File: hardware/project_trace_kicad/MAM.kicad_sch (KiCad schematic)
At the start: 2 parts, among them U501 NUCLEO-H753ZI

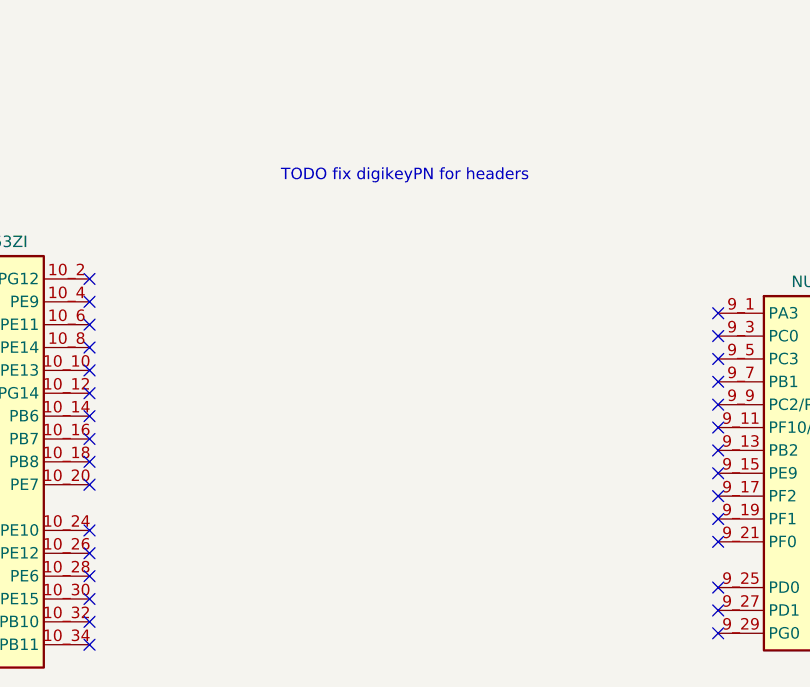
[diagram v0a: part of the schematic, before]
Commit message: Symbols for Pin-ordering added to MAM
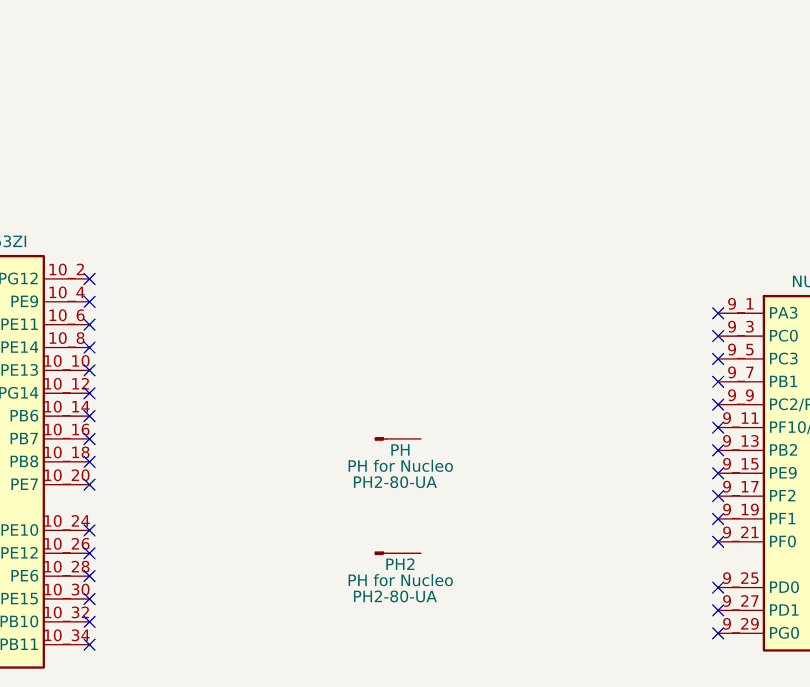
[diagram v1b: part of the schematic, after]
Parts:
- added PH, PH2: PH for Nucleo, symbol Connector:Conn_01x01_Pin
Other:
- note removed: "TODO fix digikeyPN for headers"
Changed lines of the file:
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@@
 		(company "Alexander N. Olsen")
-	)
-	(text "TODO fix digikeyPN for headers\n"
-		(exclude_from_sim no)
-		(at 129.032 95.25 0)
-		(effects
-			(font
-				(size 1.27 1.27)
-			)
-		)
 	)
 	(junction
@@
 	)
 	(symbol
+		(lib_name "Conn_01x01_Pin_1")
+		(lib_id "Connector:Conn_01x01_Pin")
+		(at 125.73 137.16 0)
+		(unit 1)
+		(body_style 1)
+		(exclude_from_sim no)
+		(in_bom yes)
+		(on_board no)
+		(in_pos_files yes)
+		(dnp no)
+		(property "Reference" "PH2"
+			(at 128.524 138.43 0)
+			(show_name no)
+			(do_not_autoplace no)
+			(effects
+				(font
+					(size 1.27 1.27)
+				)
+			)
+		)
+		(property "Value" "PH for Nucleo"
+			(at 128.524 140.208 0)
+			(show_name no)
+			(do_not_autoplace no)
+			(effects
+				(font
+					(size 1.27 1.27)
+				)
+			)
+		)
+		(property "Footprint" ""
+			(at 125.73 137.16 0)
+			(hide yes)
+			(show_name no)
+			(do_not_autoplace no)
+			(effects
+				(font
+					(size 1.27 1.27)
+				)
+			)
+		)
+		(property "Datasheet" ""
+			(at 125.73 137.16 0)
+			(hide yes)
+			(show_name no)
+			(do_not_autoplace no)
+			(effects
+				(font
+					(size 1.27 1.27)
+				)
+			)
+		)
+		(property "Description" "PH2-80-UA"
+			(at 127.889 142.0044 0)
+			(show_name no)
+			(do_not_autoplace no)
+			(effects
+				(font
+					(size 1.27 1.27)
+				)
+			)
+		)
+		(property "DIgikeyPN" "2057-PH2-80-UA-ND"
+			(at 125.73 137.16 0)
+			(hide yes)
+			(show_name no)
+			(do_not_autoplace no)
+			(effects
+				(font
+					(size 1.27 1.27)
+				)
+			)
+		)
+		(pin "1"
+		)
+		(instances
+			(project "project_trace_kicad"
+				(path "/af51f4e5-b952-4b0e-baf2-78a72fb86fcd/aebaf62e-54ce-46f5-a91f-d86d07c0b2fa"
+					(reference "PH2")
+					(unit 1)
+				)
+			)
+		)
+	)
+	(symbol
 		(lib_name "NUCLEO-H753ZI_Module_2")
 		(lib_id "ProjectTraceSymbols:NUCLEO-H753ZI_Module")
@@
 				)
 			)
+		)
+	)
+	(symbol
+		(lib_id "Connector:Conn_01x01_Pin")
+		(at 125.73 124.46 0)
+		(unit 1)
+		(body_style 1)
+		(exclude_from_sim no)
+		(in_bom yes)
+		(on_board no)
+		(in_pos_files yes)
+		(dnp no)
+		(property "Reference" "PH"
+			(at 128.524 125.73 0)
+			(show_name no)
+			(do_not_autoplace no)
+			(effects
+				(font
+					(size 1.27 1.27)
+				)
+			)
+		)
+		(property "Value" "PH for Nucleo"
+			(at 128.524 127.508 0)
+			(show_name no)
+			(do_not_autoplace no)
+			(effects
+				(font
+					(size 1.27 1.27)
+				)
+			)
+		)
+		(property "Footprint" ""
+			(at 125.73 124.46 0)
+			(hide yes)
+			(show_name no)
+			(do_not_autoplace no)
+			(effects
+				(font
+					(size 1.27 1.27)
+				)
+			)
+		)
+		(property "Datasheet" ""
+			(at 125.73 124.46 0)
+			(hide yes)
+			(show_name no)
+			(do_not_autoplace no)
+			(effects
+				(font
+					(size 1.27 1.27)
+				)
+			)
+		)
+		(property "Description" "PH2-80-UA"
+			(at 127.889 129.3044 0)
+			(show_name no)
+			(do_not_autoplace no)
+			(effects
+				(font
+					(size 1.27 1.27)
+				)
+			)
+		)
+		(property "DIgikeyPN" "2057-PH2-80-UA-ND"
+			(at 125.73 124.46 0)
+			(hide yes)
+			(show_name no)
+			(do_not_autoplace no)
+			(effects
+				(font
+					(size 1.27 1.27)
+				)
+			)
+		)
+		(pin "1"
+		)
+		(instances
+			(project "project_trace_kicad"
+				(path "/af51f4e5-b952-4b0e-baf2-78a72fb86fcd/aebaf62e-54ce-46f5-a91f-d86d07c0b2fa"
+					(reference "PH")
+					(unit 1)
+				)
+			)

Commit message: Work on PCB
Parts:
- renumbered PH to PH501, PH2 to PH502
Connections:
- no-connect marks 67 -> 69
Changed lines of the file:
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@@
+	)
+	(no_connect
+		(at 130.81 124.46)
 	)
 	(no_connect
@@
 	(no_connect
 		(at 194.31 128.27)
+	)
+	(no_connect
+		(at 130.81 137.16)
 	)
 	(no_connect
@@
 		(in_pos_files yes)
 		(dnp no)
-		(property "Reference" "PH2"
+		(property "Reference" "PH502"
 			(at 128.524 138.43 0)
 			(show_name no)
@@
 			(project "project_trace_kicad"
 				(path "/af51f4e5-b952-4b0e-baf2-78a72fb86fcd/aebaf62e-54ce-46f5-a91f-d86d07c0b2fa"
-					(reference "PH2")
+					(reference "PH502")
 					(unit 1)
 				)
@@
 		(in_pos_files yes)
 		(dnp no)
-		(property "Reference" "PH"
+		(property "Reference" "PH501"
 			(at 128.524 125.73 0)
 			(show_name no)
@@
 			(project "project_trace_kicad"
 				(path "/af51f4e5-b952-4b0e-baf2-78a72fb86fcd/aebaf62e-54ce-46f5-a91f-d86d07c0b2fa"
-					(reference "PH")
+					(reference "PH501")
 					(unit 1)
 				)

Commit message: Partnumbers and BOM updated
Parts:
- PH501, PH502: DIgikeyPN 2057-PH2-80-UA-ND -> (none); DigikeyPN (none) -> 2057-PH2-80-UA-ND
- U501: DigikeyPN 2057-PH2-80-UA-ND AND 2057-PH2-20-UA-ND -> (none)
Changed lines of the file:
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@@
-			)
-		)
-		(property "DigikeyPN" "2057-PH2-80-UA-ND AND 2057-PH2-20-UA-ND"
-			(at 77.47 49.53 0)
-			(hide yes)
-			(show_name no)
-			(do_not_autoplace no)
-			(effects
-				(font
-					(size 1.27 1.27)
-				)
 			)
 		)
@@
 			)
 		)
-		(property "DIgikeyPN" "2057-PH2-80-UA-ND"
+		(property "DigikeyPN" "2057-PH2-80-UA-ND"
 			(at 125.73 137.16 0)
 			(hide yes)
@@
 			)
 		)
-		(property "DigikeyPN" "2057-PH2-80-UA-ND AND 2057-PH2-20-UA-ND"
-			(at 179.07 128.27 0)
-			(hide yes)
-			(show_name no)
-			(do_not_autoplace no)
-			(effects
-				(font
-					(size 1.27 1.27)
-				)
-			)
-		)
 		(pin "9_12"
 		)
@@
 		(property "Description" "Nucleo 144 Development Board with STM32F429ZIT6 MCU, 256kB RAM, 1Mb FLASH"
 			(at 147.32 -49.53 0)
-			(hide yes)
-			(show_name no)
-			(do_not_autoplace no)
-			(effects
-				(font
-					(size 1.27 1.27)
-				)
-			)
-		)
-		(property "DigikeyPN" "2057-PH2-80-UA-ND AND 2057-PH2-20-UA-ND"
-			(at 147.32 52.07 0)
 			(hide yes)
 			(show_name no)
@@
 			)
 		)
-		(property "DigikeyPN" "2057-PH2-80-UA-ND AND 2057-PH2-20-UA-ND"
-			(at 80.01 127 0)
-			(hide yes)
-			(show_name no)
-			(do_not_autoplace no)
-			(effects
-				(font
-					(size 1.27 1.27)
-				)
-			)
-		)
 		(pin "9_12"
 		)
@@
 			)
 		)
-		(property "DigikeyPN" "2057-PH2-80-UA-ND AND 2057-PH2-20-UA-ND"
-			(at 213.36 55.88 0)
-			(hide yes)
-			(show_name no)
-			(do_not_autoplace no)
-			(effects
-				(font
-					(size 1.27 1.27)
-				)
-			)
-		)
 		(pin "9_12"
 		)
@@
 			)
 		)
-		(property "DIgikeyPN" "2057-PH2-80-UA-ND"
+		(property "DigikeyPN" "2057-PH2-80-UA-ND"
 			(at 125.73 124.46 0)
 			(hide yes)

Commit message: Improvements to PCB
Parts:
- R501: value 100 -> 24R9; footprint ProjectTraceFootprints:RN73R2ATTD1000B25 -> Resistor_SMD:R_0603_1608Metric_Pad0.98x0.95mm_HandSolder; DigikeyPN 2019-RN73R2ATTD1000B25CT-ND -> YAG4511CT-ND
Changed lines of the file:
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@@
+	)
+	(symbol
+		(lib_id "Device:R")
+		(at 242.57 49.53 90)
+		(unit 1)
+		(body_style 1)
+		(exclude_from_sim no)
+		(in_bom yes)
+		(on_board yes)
+		(in_pos_files yes)
+		(dnp no)
+		(fields_autoplaced yes)
+		(property "Reference" "R501"
+			(at 242.57 44.7546 90)
+			(show_name no)
+			(do_not_autoplace no)
+			(effects
+				(font
+					(size 1.27 1.27)
+				)
+			)
+		)
+		(property "Value" "24R9"
+			(at 242.57 46.9222 90)
+			(show_name no)
+			(do_not_autoplace no)
+			(effects
+				(font
+					(size 1.27 1.27)
+				)
+			)
+		)
+		(property "Footprint" "Resistor_SMD:R_0603_1608Metric_Pad0.98x0.95mm_HandSolder"
+			(at 242.57 51.308 90)
+			(hide yes)
+			(show_name no)
+			(do_not_autoplace no)
+			(effects
+				(font
+					(size 1.27 1.27)
+				)
+			)
+		)
+		(property "Datasheet" ""
+			(at 242.57 49.53 0)
+			(hide yes)
+			(show_name no)
+			(do_not_autoplace no)
+			(effects
+				(font
+					(size 1.27 1.27)
+				)
+			)
+		)
+		(property "Description" "Resistor"
+			(at 242.57 49.53 0)
+			(hide yes)
+			(show_name no)
+			(do_not_autoplace no)
+			(effects
+				(font
+					(size 1.27 1.27)
+				)
+			)
+		)
+		(property "DigikeyPN" "YAG4511CT-ND"
+			(at 242.57 49.53 90)
+			(hide yes)
+			(show_name no)
+			(do_not_autoplace no)
+			(effects
+				(font
+					(size 1.27 1.27)
+				)
+			)
+		)
+		(pin "1"
+		)
+		(pin "2"
+		)
+		(instances
+			(project "project_trace_kicad"
+				(path "/af51f4e5-b952-4b0e-baf2-78a72fb86fcd/aebaf62e-54ce-46f5-a91f-d86d07c0b2fa"
+					(reference "R501")
+					(unit 1)
+				)
+			)
+		)
 	)
 	(symbol
@@
 					(unit 1)
 				)
-			)
-		)
-	)
-	(symbol
-		(lib_id "Device:R")
-		(at 242.57 49.53 90)
-		(unit 1)
-		(body_style 1)
-		(exclude_from_sim no)
-		(in_bom yes)
-		(on_board yes)
-		(in_pos_files yes)
-		(dnp no)
-		(fields_autoplaced yes)
-		(property "Reference" "R501"
-			(at 242.57 44.3695 90)
-			(show_name no)
-			(do_not_autoplace no)
-			(effects
-				(font
-					(size 1.27 1.27)
-				)
-			)
-		)
-		(property "Value" "100"
-			(at 242.57 46.7938 90)
-			(show_name no)
-			(do_not_autoplace no)
-			(effects
-				(font
-					(size 1.27 1.27)
-				)
-			)
-		)
-		(property "Footprint" "ProjectTraceFootprints:RN73R2ATTD1000B25"
-			(at 242.57 51.308 90)
-			(hide yes)
-			(show_name no)
-			(do_not_autoplace no)
-			(effects
-				(font
-					(size 1.27 1.27)
-				)
-			)
-		)
-		(property "Datasheet" ""
-			(at 242.57 49.53 0)
-			(hide yes)
-			(show_name no)
-			(do_not_autoplace no)
-			(effects
-				(font
-					(size 1.27 1.27)
-				)
-			)
-		)
-		(property "Description" "Resistor"
-			(at 242.57 49.53 0)
-			(hide yes)
-			(show_name no)
-			(do_not_autoplace no)
-			(effects
-				(font
-					(size 1.27 1.27)
-				)
-			)
-		)
-		(property "DigikeyPN" "2019-RN73R2ATTD1000B25CT-ND"
-			(at 242.57 49.53 90)
-			(hide yes)
-			(show_name no)
-			(do_not_autoplace no)
-			(effects
-				(font
-					(size 1.27 1.27)
-				)
-			)
-		)
-		(pin "1"
-		)
-		(pin "2"
-		)
-		(instances
-			(project "project_trace_kicad"
-				(path "/af51f4e5-b952-4b0e-baf2-78a72fb86fcd/aebaf62e-54ce-46f5-a91f-d86d07c0b2fa"
-					(reference "R501")
-					(unit 1)
-				)

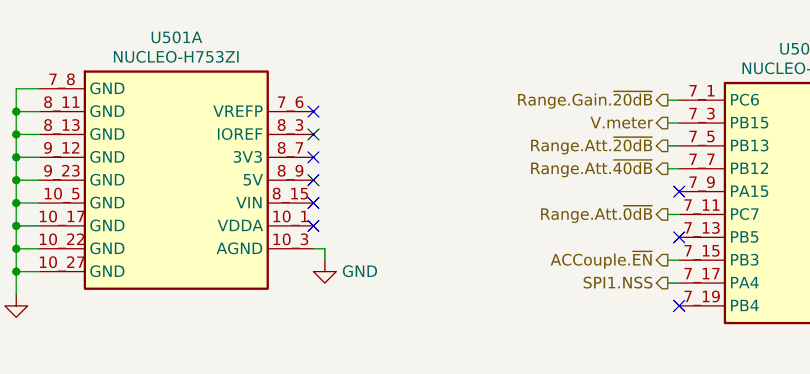
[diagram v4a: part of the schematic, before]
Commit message: Add Missing Power Connection to Nucleo
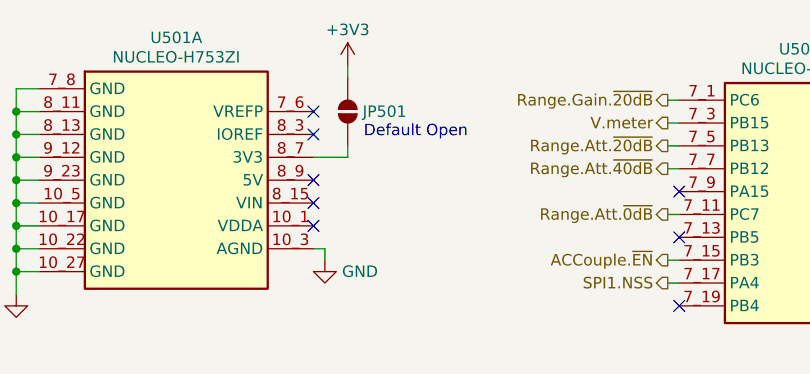
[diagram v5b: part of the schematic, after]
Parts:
- added JP501: SolderJumper_2_Open, Jumper:SolderJumper-2_P1.3mm_Open_RoundedPad1.0x1.5mm, symbol Jumper:SolderJumper_2_Open
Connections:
- net at U501.8_7 (3V3): now also JP501.2 (B)
- new net +3V3: JP501.1 (A)
- no-connect marks 69 -> 68
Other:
- note added: "Default Open"
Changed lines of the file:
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@@
 		(company "Alexander N. Olsen")
+	)
+	(text "Default Open"
+		(exclude_from_sim no)
+		(at 98.298 44.196 0)
+		(effects
+			(font
+				(size 1.27 1.27)
+			)
+			(justify left)
+		)
 	)
 	(junction
@@
 	)
 	(no_connect
-		(at 92.71 46.99)
-	)
-	(no_connect
 		(at 161.29 43.18)
 	)
@@
 	(wire
 		(pts
+			(xy 96.52 36.83) (xy 96.52 38.1)
+		)
+		(stroke
+			(width 0)
+			(type default)
+		)
+	)
+	(wire
+		(pts
 			(xy 59.69 54.61) (xy 59.69 57.15)
 		)
@@
 	(wire
 		(pts
+			(xy 96.52 45.72) (xy 96.52 46.99)
+		)
+		(stroke
+			(width 0)
+			(type default)
+		)
+	)
+	(wire
+		(pts
 			(xy 227.33 49.53) (xy 238.76 49.53)
 		)
@@
 		(pts
 			(xy 59.69 39.37) (xy 62.23 39.37)
+		)
+		(stroke
+			(width 0)
+			(type default)
+		)
+	)
+	(wire
+		(pts
+			(xy 96.52 46.99) (xy 92.71 46.99)
 		)
 		(stroke
@@
 				(path "/af51f4e5-b952-4b0e-baf2-78a72fb86fcd/aebaf62e-54ce-46f5-a91f-d86d07c0b2fa"
 					(reference "R501")
+					(unit 1)
+				)
+			)
+		)
+	)
+	(symbol
+		(lib_id "Jumper:SolderJumper_2_Open")
+		(at 96.52 41.91 270)
+		(unit 1)
+		(body_style 1)
+		(exclude_from_sim no)
+		(in_bom no)
+		(on_board yes)
+		(in_pos_files yes)
+		(dnp no)
+		(fields_autoplaced yes)
+		(property "Reference" "JP501"
+			(at 98.171 41.91 90)
+			(show_name no)
+			(do_not_autoplace no)
+			(effects
+				(font
+					(size 1.27 1.27)
+				)
+				(justify left)
+			)
+		)
+		(property "Value" "SolderJumper_2_Open"
+			(at 94.869 40.8262 90)
+			(hide yes)
+			(show_name no)
+			(do_not_autoplace no)
+			(effects
+				(font
+					(size 1.27 1.27)
+				)
+				(justify right)
+			)
+		)
+		(property "Footprint" "Jumper:SolderJumper-2_P1.3mm_Open_RoundedPad1.0x1.5mm"
+			(at 96.52 41.91 0)
+			(hide yes)
+			(show_name no)
+			(do_not_autoplace no)
+			(effects
+				(font
+					(size 1.27 1.27)
+				)
+			)
+		)
+		(property "Datasheet" ""
+			(at 96.52 41.91 0)
+			(hide yes)
+			(show_name no)
+			(do_not_autoplace no)
+			(effects
+				(font
+					(size 1.27 1.27)
+				)
+			)
+		)
+		(property "Description" "Solder Jumper, 2-pole, open"
+			(at 96.52 41.91 0)
+			(hide yes)
+			(show_name no)
+			(do_not_autoplace no)
+			(effects
+				(font
+					(size 1.27 1.27)
+				)
+			)
+		)
+		(property "DigikeyPN" "N/A"
+			(at 96.52 41.91 90)
+			(hide yes)
+			(show_name no)
+			(do_not_autoplace no)
+			(effects
+				(font
+					(size 1.27 1.27)
+				)
+			)
+		)
+		(pin "1"
+		)
+		(pin "2"
+		)
+		(instances
+			(project "project_trace_kicad"
+				(path "/af51f4e5-b952-4b0e-baf2-78a72fb86fcd/aebaf62e-54ce-46f5-a91f-d86d07c0b2fa"
+					(reference "JP501")
 					(unit 1)
 				)
@@
 					(unit 1)
 				)
+			)
+		)
+	)
+	(symbol
+		(lib_id "power:+3V3")
+		(at 96.52 36.83 0)
+		(unit 1)
+		(body_style 1)
+		(exclude_from_sim no)
+		(in_bom yes)
+		(on_board yes)
+		(in_pos_files yes)
+		(dnp no)
+		(fields_autoplaced yes)
+		(property "Reference" "#PWR0503"
+			(at 96.52 40.64 0)
+			(hide yes)
+			(show_name no)
+			(do_not_autoplace no)
+			(effects
+				(font
+					(size 1.27 1.27)
+				)
+			)
+		)
+		(property "Value" "+3V3"
+			(at 96.52 32.8252 0)
+			(show_name no)
+			(do_not_autoplace no)
+			(effects
+				(font
+					(size 1.27 1.27)
+				)
+			)
+		)
+		(property "Footprint" ""
+			(at 96.52 36.83 0)
+			(hide yes)
+			(show_name no)
+			(do_not_autoplace no)
+			(effects
+				(font
+					(size 1.27 1.27)
+				)
+			)
+		)
+		(property "Datasheet" ""
+			(at 96.52 36.83 0)
+			(hide yes)
+			(show_name no)
+			(do_not_autoplace no)
+			(effects
+				(font
+					(size 1.27 1.27)
+				)
+			)
+		)
+		(property "Description" "Power symbol creates a global label with name \"+3V3\""
+			(at 96.52 36.83 0)
+			(hide yes)
+			(show_name no)
+			(do_not_autoplace no)
+			(effects
+				(font
+					(size 1.27 1.27)
+				)
+			)
+		)
+		(pin "1"
+		)
+		(instances
+			(project "project_trace_kicad"
+				(path "/af51f4e5-b952-4b0e-baf2-78a72fb86fcd/aebaf62e-54ce-46f5-a91f-d86d07c0b2fa"
+					(reference "#PWR0503")
+					(unit 1)
+				)

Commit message: Rework started
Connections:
- net SW3.A: now also U501.7_12 (PA6); no longer U501.9_24 (PF8)
- net SW3.B: now also U501.9_7 (PB1); no longer U501.9_26 (PF7)
- net SW4.A: now also U501.10_33 (PE0); no longer U501.9_28 (PF9)
- net SW4.B: now also U501.9_1 (PA3); no longer U501.9_30 (PG1)
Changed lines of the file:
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@@
-	)
-	(no_connect
-		(at 161.29 53.34)
 	)
 	(no_connect
@@
 	)
 	(no_connect
-		(at 66.04 139.7)
-	)
-	(no_connect
 		(at 93.98 114.3)
 	)
@@
 	)
 	(no_connect
+		(at 194.31 138.43)
+	)
+	(no_connect
 		(at 163.83 123.19)
 	)
@@
 	)
 	(no_connect
-		(at 163.83 110.49)
-	)
-	(no_connect
 		(at 194.31 113.03)
 	)
@@
 	)
 	(no_connect
+		(at 194.31 143.51)
+	)
+	(no_connect
 		(at 161.29 63.5)
 	)
@@
 	)
 	(no_connect
+		(at 194.31 140.97)
+	)
+	(no_connect
 		(at 66.04 134.62)
 	)
@@
 	)
 	(no_connect
-		(at 163.83 118.11)
+		(at 194.31 146.05)
 	)
 	(no_connect
@@
 	(wire
 		(pts
-			(xy 194.31 138.43) (xy 198.12 138.43)
+			(xy 161.29 53.34) (xy 163.83 53.34)
 		)
 		(stroke
@@
 	(wire
 		(pts
-			(xy 194.31 143.51) (xy 198.12 143.51)
+			(xy 66.04 139.7) (xy 64.77 139.7)
 		)
 		(stroke
@@
 	(wire
 		(pts
-			(xy 194.31 140.97) (xy 198.12 140.97)
+			(xy 163.83 118.11) (xy 162.56 118.11)
 		)
 		(stroke
@@
 	(wire
 		(pts
-			(xy 194.31 146.05) (xy 198.12 146.05)
+			(xy 163.83 110.49) (xy 162.56 110.49)
 		)
 		(stroke
@@
 	(hierarchical_label "SW4.A"
 		(shape input)
-		(at 198.12 143.51 0)
-		(effects
-			(font
-				(size 1.27 1.27)
-			)
-			(justify left)
+		(at 64.77 139.7 180)
+		(effects
+			(font
+				(size 1.27 1.27)
+			)
+			(justify right)
 		)
 	)
@@
 	(hierarchical_label "SW3.B"
 		(shape input)
-		(at 198.12 140.97 0)
-		(effects
-			(font
-				(size 1.27 1.27)
-			)
-			(justify left)
+		(at 162.56 118.11 180)
+		(effects
+			(font
+				(size 1.27 1.27)
+			)
+			(justify right)
 		)
 	)
@@
 	(hierarchical_label "SW4.B"
 		(shape input)
-		(at 198.12 146.05 0)
-		(effects
-			(font
-				(size 1.27 1.27)
-			)
-			(justify left)
+		(at 162.56 110.49 180)
+		(effects
+			(font
+				(size 1.27 1.27)
+			)
+			(justify right)
 		)
 	)
 	(hierarchical_label "SW3.A"
 		(shape input)
-		(at 198.12 138.43 0)
-		(effects
-			(font
+		(at 163.83 53.34 0)
+		(effects
+			(font

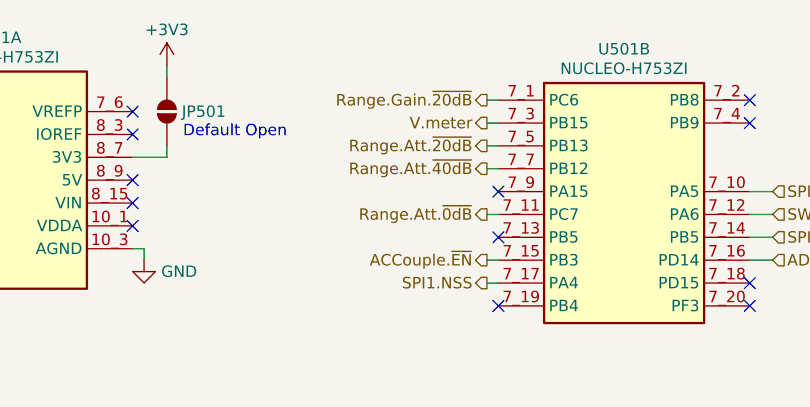
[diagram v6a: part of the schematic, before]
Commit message: Fix inconsistency with ADC datasheet, fix DRC Errors
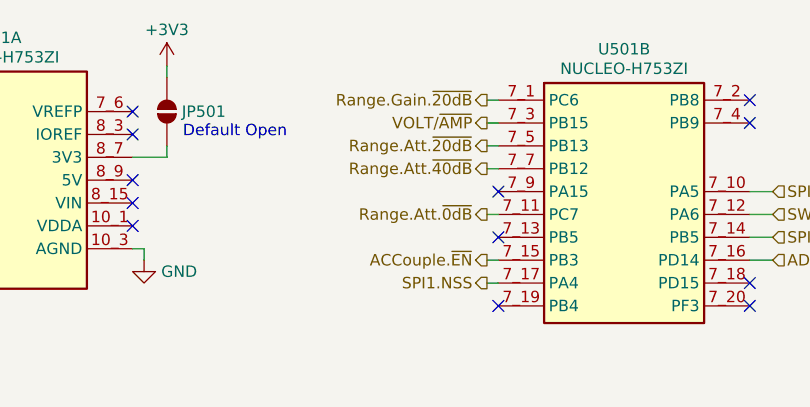
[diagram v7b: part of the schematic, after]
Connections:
- net V.meter renamed VOLT/~{AMP}
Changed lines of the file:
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@@
 		)
 	)
-	(hierarchical_label "V.meter"
+	(hierarchical_label "VOLT{slash}~{AMP}"
 		(shape output)
 		(at 132.08 43.18 180)
